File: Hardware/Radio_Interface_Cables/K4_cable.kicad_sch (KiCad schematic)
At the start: 2 parts, among them J16 RJ45, J17 DE15_Socket_HighDensity

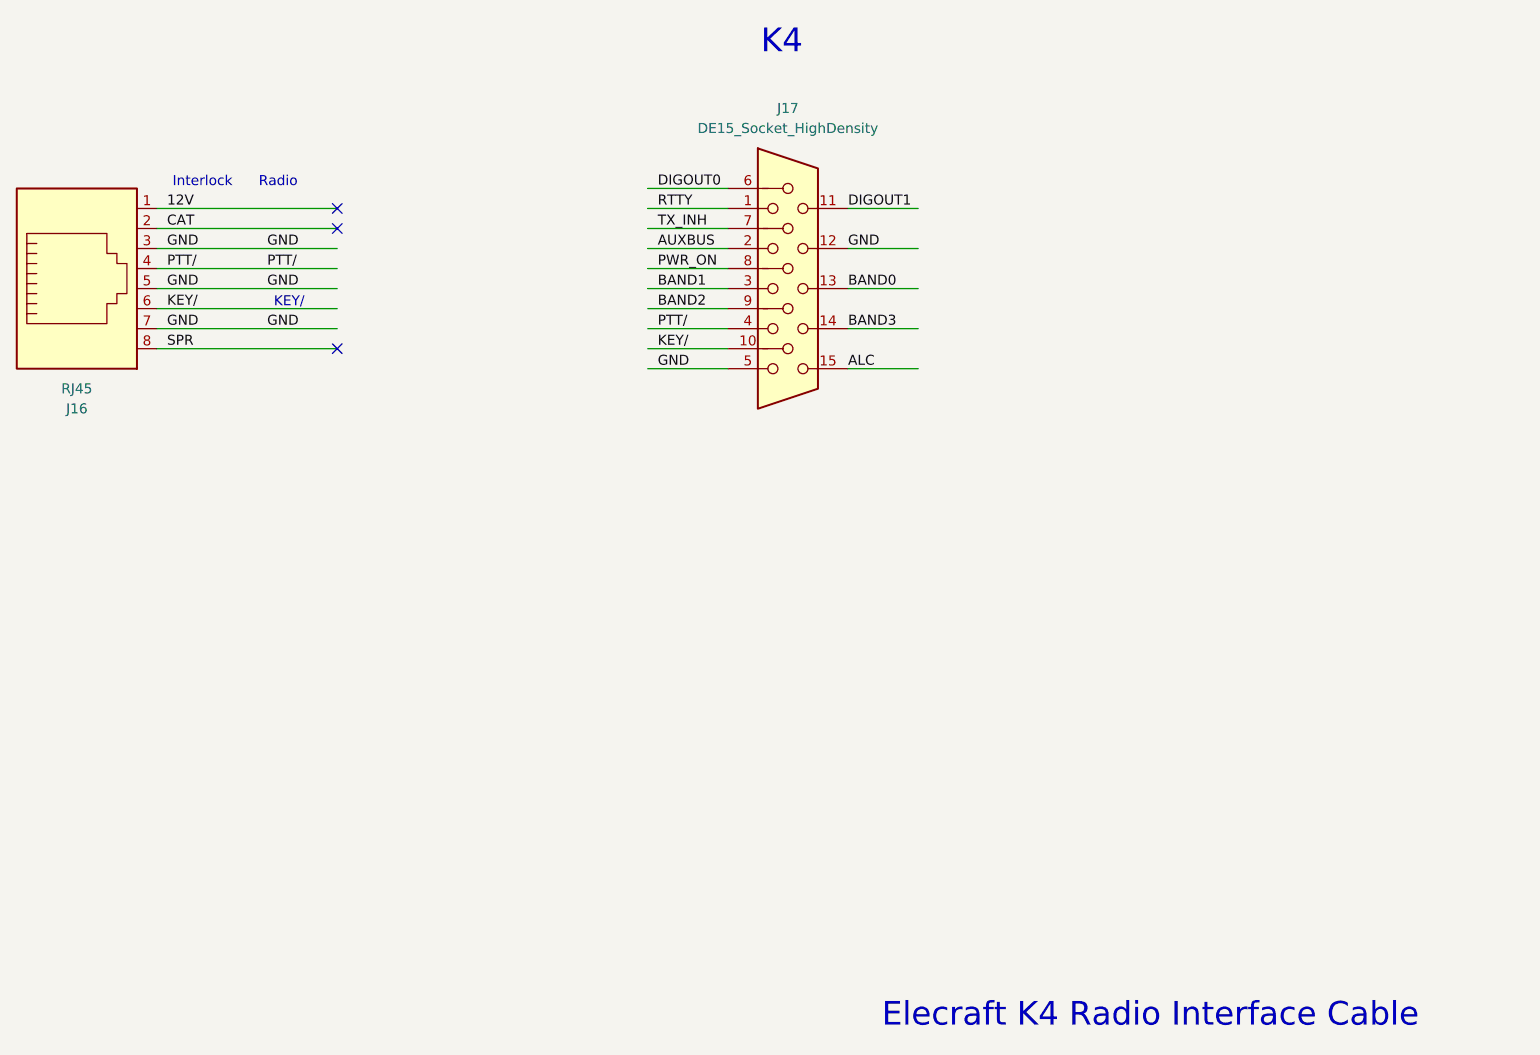
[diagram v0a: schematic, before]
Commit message: Add PTT and CAT connectors on Radio Interface Cables Mark pins as unused
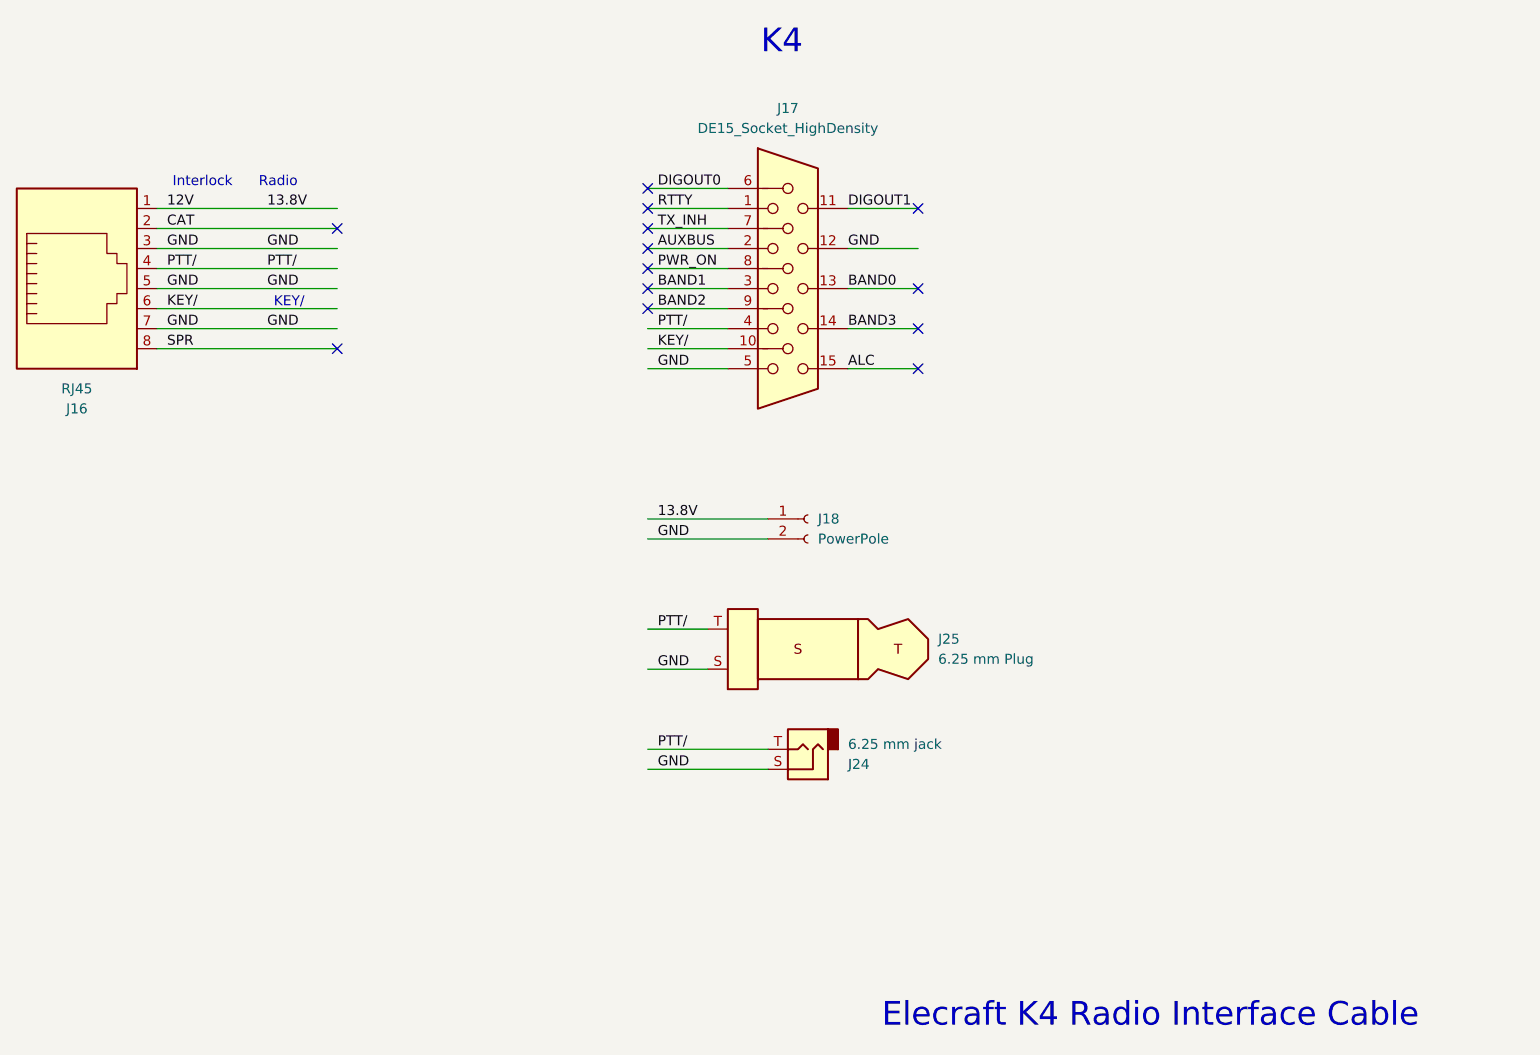
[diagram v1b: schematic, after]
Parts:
- added J18: PowerPole, symbol Connector:Conn_01x02_Socket
- added J24: 6.25 mm jack, symbol Connector_Audio:AudioJack2
- added J25: 6.25 mm Plug, symbol Connector_Audio:AudioPlug2
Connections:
- net 12V: now also J18.1 (Pin_1)
- net GND: now also J18.2 (Pin_2), J24.S, J25.S
- net PTT/: now also J24.T, J25.T
- no-connect marks 3 -> 13
